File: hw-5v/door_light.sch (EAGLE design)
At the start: 30 parts, among them IC1 TINY13-20SSU, Q1 BSP250, T1 n-mosfet, T2 KP-3216P3C, U1 MC33063ADE4

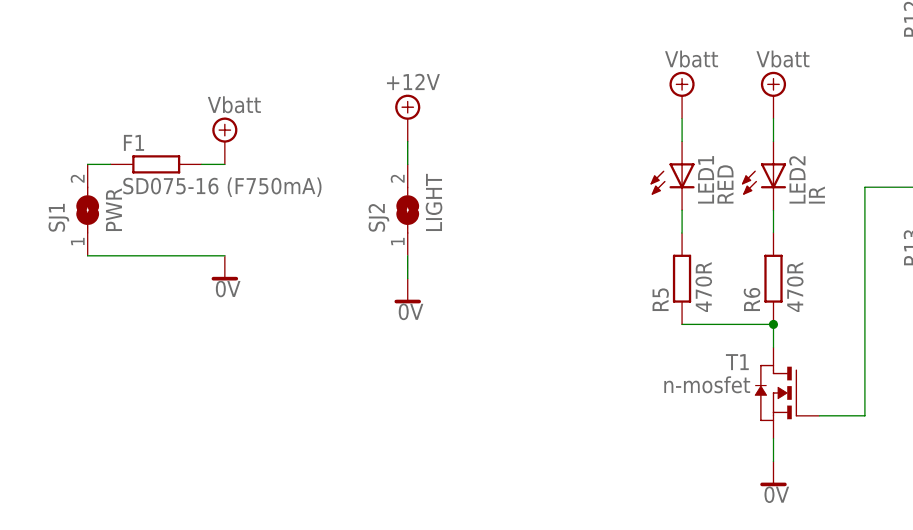
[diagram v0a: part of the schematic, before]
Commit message: fixed few not-so-bright-namings on the schemas
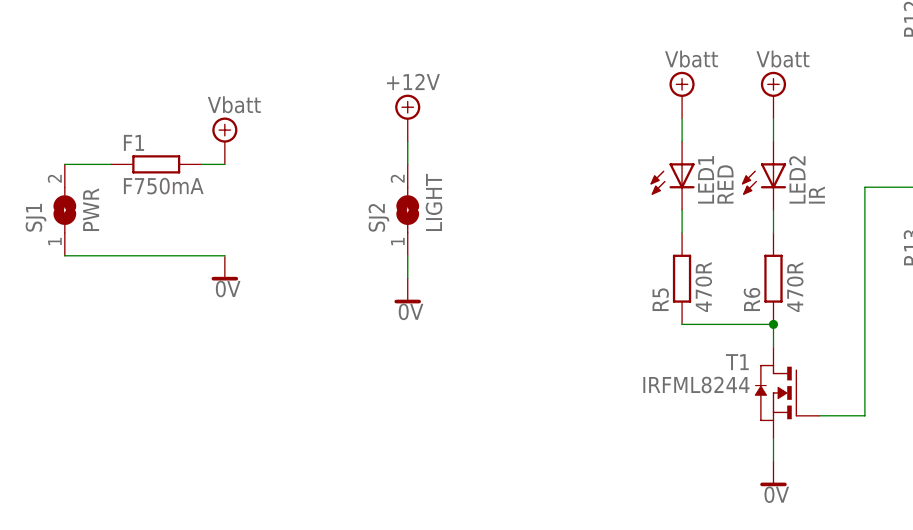
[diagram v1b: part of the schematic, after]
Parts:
- F1: value SD075-16 (F750mA) -> F750mA
- T1: value n-mosfet -> IRFML8244
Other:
- moved on the sheet: SJ1
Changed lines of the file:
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@@
 <part name="U1" library="Texas Instruments_By_element14_Batch_1" deviceset="MC33063ADE4" device=""/>
 <part name="SUPPLY26" library="supply2" deviceset="+4.1V" device="" value="Vbatt"/>
-<part name="F1" library="rcl" deviceset="R-EU_" device="MELF0204W" value="SD075-16 (F750mA)"/>
+<part name="F1" library="rcl" deviceset="R-EU_" device="MELF0204W" value="F750mA"/>
 <part name="R7" library="rcl" deviceset="R-EU_" device="R0402" value="10kR"/>
 <part name="D1" library="diode" deviceset="MBRS130LT3" device="" value=" MBRS140T3G"/>
@@
 <part name="SUPPLY28" library="supply2" deviceset="0V" device=""/>
 <part name="Q1" library="transistor-fet" deviceset="BSP170P" device="" value="BSP250"/>
-<part name="T1" library="zetex" deviceset="NMOSSOT23" device="" value="n-mosfet"/>
+<part name="T1" library="zetex" deviceset="NMOSSOT23" device="" value="IRFML8244"/>
 <part name="SJ1" library="jumper" deviceset="SJ" device="W" value="PWR"/>
 <part name="SJ2" library="jumper" deviceset="SJ" device="W" value="LIGHT"/>
@@
 <instance part="Q1" gate="G$1" x="-38.1" y="144.78"/>
 <instance part="T1" gate="A" x="30.48" y="15.24" rot="MR0"/>
-<instance part="SJ1" gate="1" x="-45.72" y="35.56" rot="R90"/>
+<instance part="SJ1" gate="1" x="-48.26" y="35.56" rot="R90"/>
 <instance part="SJ2" gate="1" x="-10.16" y="35.56" rot="R90"/>
 <instance part="R12" gate="G$1" x="48.26" y="58.42" rot="R90"/>
@@
 <pinref part="SJ1" gate="1" pin="1"/>
 <pinref part="SUPPLY14" gate="0V" pin="0V"/>
-<wire x1="-30.48" y1="30.48" x2="-45.72" y2="30.48" width="0.1524" layer="91"/>
+<wire x1="-30.48" y1="30.48" x2="-48.26" y2="30.48" width="0.1524" layer="91"/>
 </segment>
 <segment>
@@
 <segment>
 <pinref part="F1" gate="G$1" pin="1"/>
-<wire x1="-43.18" y1="40.64" x2="-45.72" y2="40.64" width="0.1524" layer="91"/>
+<wire x1="-43.18" y1="40.64" x2="-48.26" y2="40.64" width="0.1524" layer="91"/>
 <pinref part="SJ1" gate="1" pin="2"/>
 </segment>

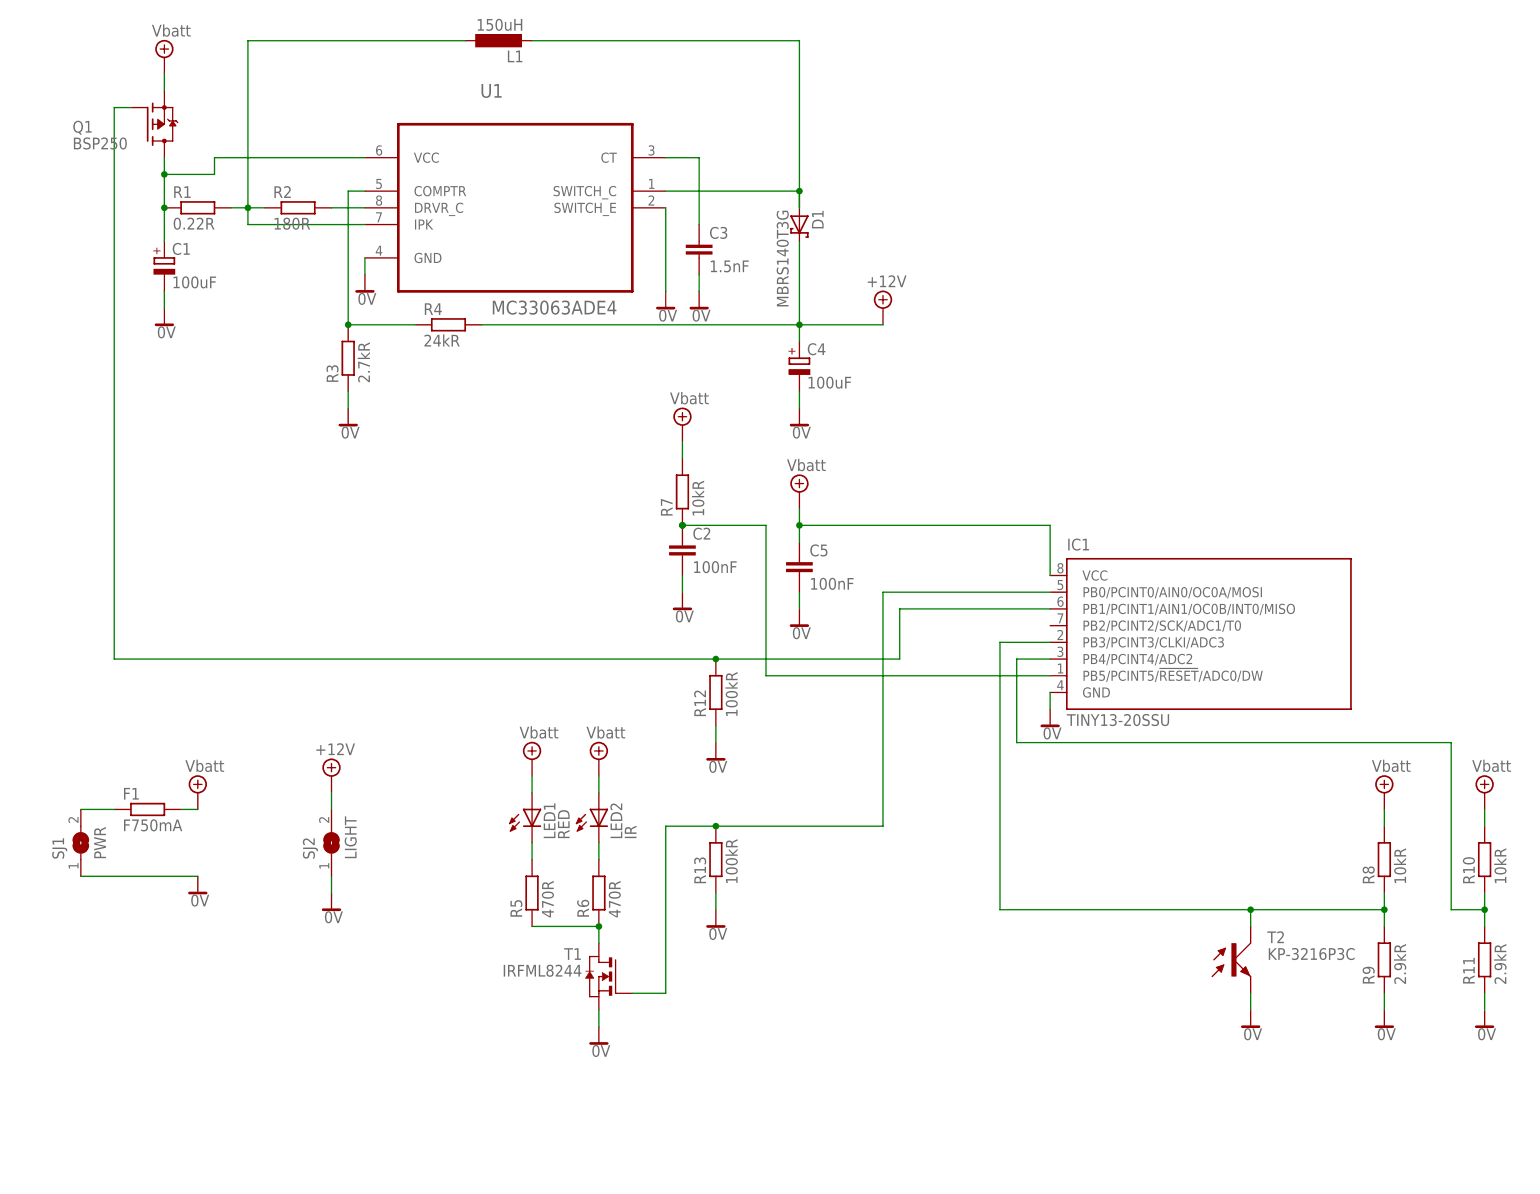
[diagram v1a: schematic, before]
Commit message: 12V version schema is ready, TODOs fixed; PCB is draft-done - to be tested and improved
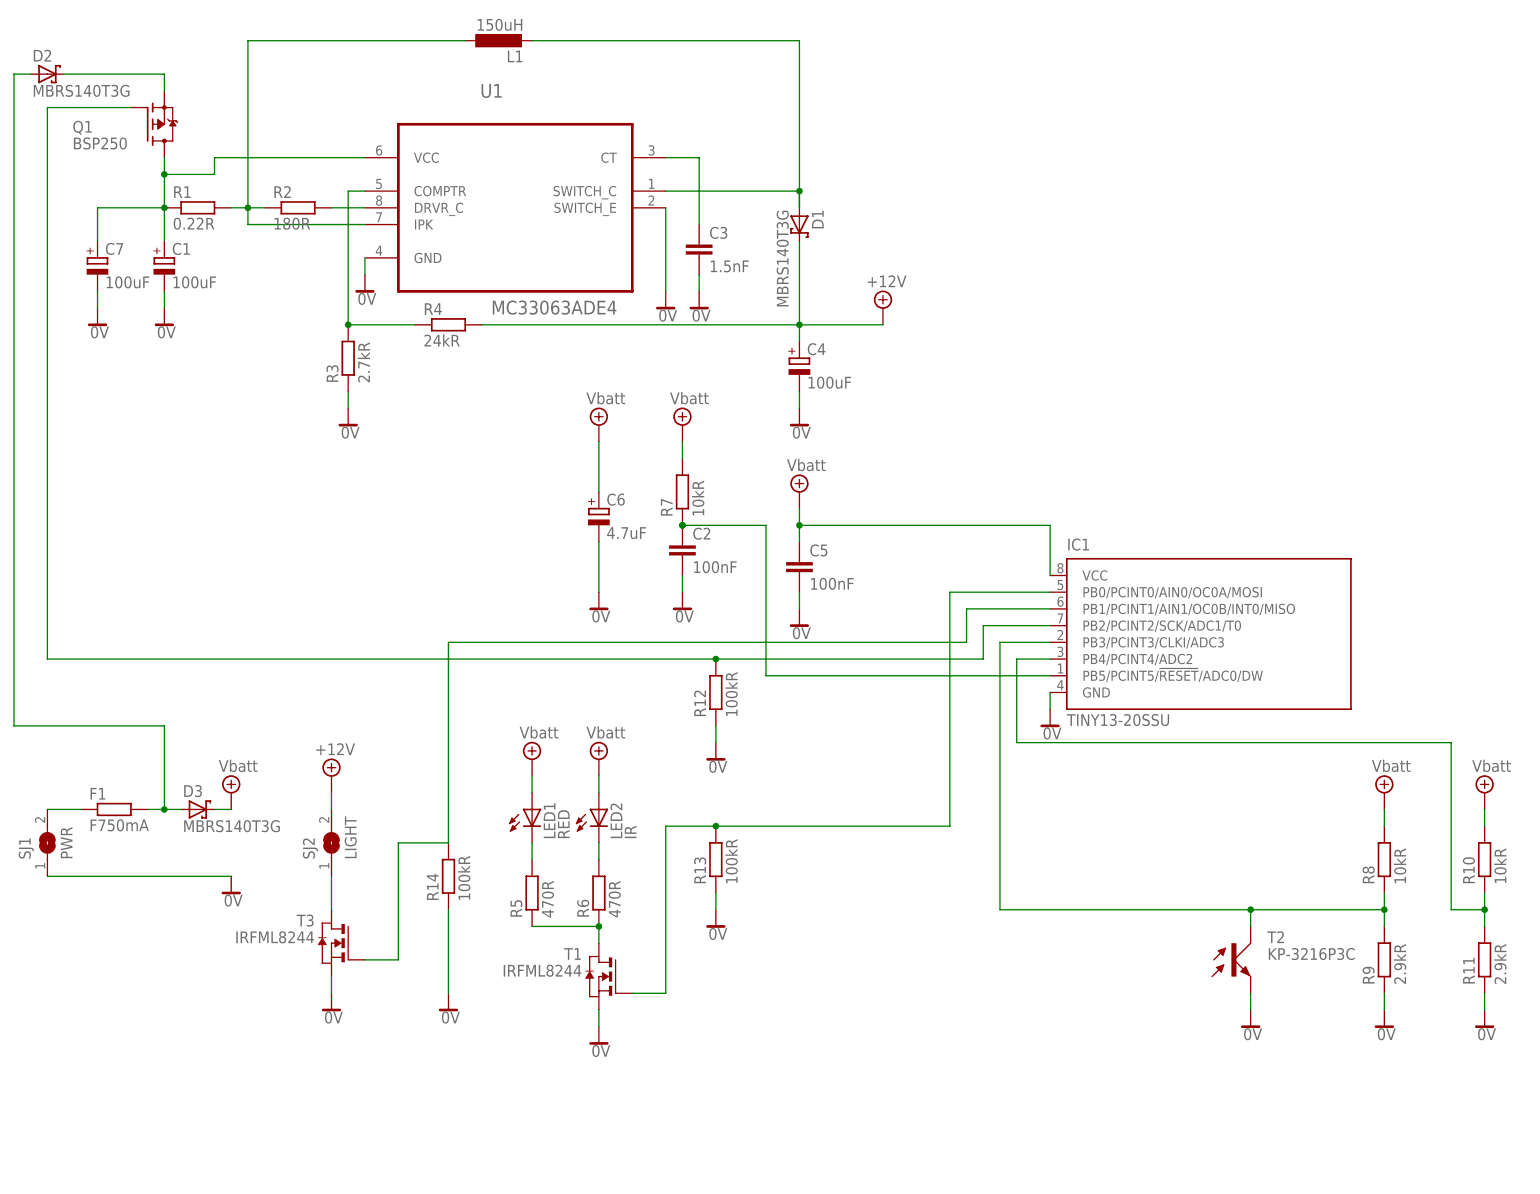
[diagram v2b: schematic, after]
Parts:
- added C6: 4.7uF, rcl:CPOL-EU153CLV-0405
- added C7: 100uF, rcl:CPOL-EU153CLV-0810
- added D2, D3: MBRS140T3G, diode:MBRS130LT3
- added R14: 100kR, rcl:R-EU_R0603
- added T3: IRFML8244, zetex:NMOSSOT23
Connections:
- new net N$19: IC1.PB1/PCINT1/AIN1/OC0B/INT0/MISO, R14.2, T3.G
- new net N$21: D2.A, D3.A, F1.2
- new net N$5: D2.C, Q1.S
- new net N$7: SJ2.1, T3.D
- net +4.1V: now also C6.+, D3.C; no longer F1.2, Q1.S
- net 0V: now also C6.-, C7.-, R14.1, T3.S; no longer SJ2.1
- net N$13: now also IC1.PB2/PCINT2/SCK/ADC1/T0; no longer IC1.PB1/PCINT1/AIN1/OC0B/INT0/MISO
- net N$3: now also C7.+
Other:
- moved on the sheet: F1, SJ1

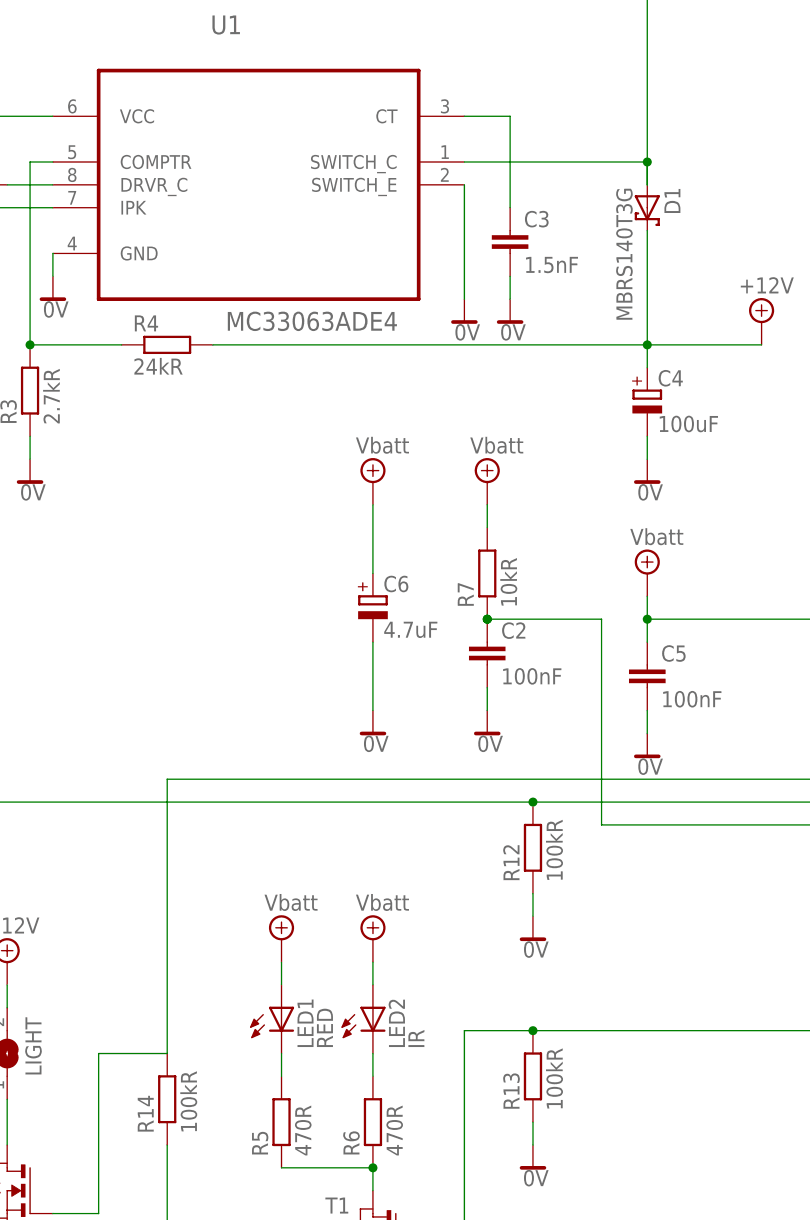
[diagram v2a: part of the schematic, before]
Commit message: route fixes; changed fuse to bigger package (1A)
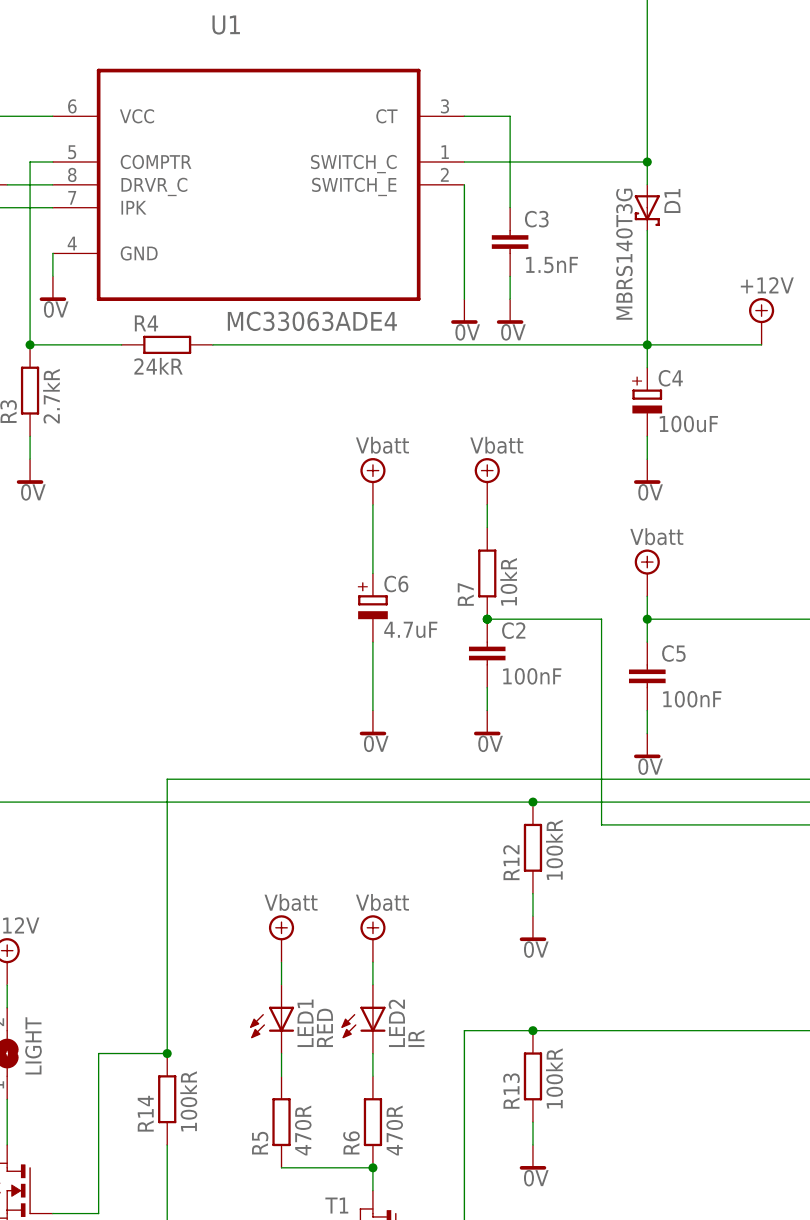
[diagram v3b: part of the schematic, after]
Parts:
- F1: device rcl:R-EU_MELF0204W -> rcl:R-EU_MELF0207W
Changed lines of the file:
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@@
 <part name="U1" library="Texas Instruments_By_element14_Batch_1" deviceset="MC33063ADE4" device=""/>
 <part name="SUPPLY26" library="supply2" deviceset="+4.1V" device="" value="Vbatt"/>
-<part name="F1" library="rcl" deviceset="R-EU_" device="MELF0204W" value="F750mA"/>
+<part name="F1" library="rcl" deviceset="R-EU_" device="MELF0207W" value="F750mA"/>
 <part name="R7" library="rcl" deviceset="R-EU_" device="R0402" value="10kR"/>
 <part name="D1" library="diode" deviceset="MBRS130LT3" device="" value=" MBRS140T3G"/>
@@
 <pinref part="U1" gate="A" pin="SWITCH_C"/>
 <wire x1="40.64" y1="134.62" x2="60.96" y2="134.62" width="0.1524" layer="91"/>
-<wire x1="60.96" y1="134.62" x2="60.96" y2="132.08" width="0.1524" layer="91"/>
 <pinref part="D1" gate="G$1" pin="A"/>
 <pinref part="L1" gate="G$1" pin="2"/>
@@
 <wire x1="99.06" y1="71.12" x2="86.36" y2="71.12" width="0.1524" layer="91"/>
 <wire x1="86.36" y1="71.12" x2="86.36" y2="66.04" width="0.1524" layer="91"/>
+<junction x="7.62" y="35.56"/>
 </segment>
 </net>
@@
 </sheet>
 </sheets>
+<errors>
+</errors>
 </schematic>
 </drawing>

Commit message: fixed invalid 10kR resistor size
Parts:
- R7: device rcl:R-EU_R0402 -> rcl:R-EU_R0603
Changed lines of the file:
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@@
 <part name="SUPPLY26" library="supply2" deviceset="+4.1V" device="" value="Vbatt"/>
 <part name="F1" library="rcl" deviceset="R-EU_" device="MELF0207W" value="F750mA"/>
-<part name="R7" library="rcl" deviceset="R-EU_" device="R0402" value="10kR"/>
+<part name="R7" library="rcl" deviceset="R-EU_" device="R0603" value="10kR"/>
 <part name="D1" library="diode" deviceset="MBRS130LT3" device="" value=" MBRS140T3G"/>
 <part name="C3" library="rcl" deviceset="C-EU" device="C1206" value="1.5nF"/>
